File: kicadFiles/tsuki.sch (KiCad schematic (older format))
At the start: 332 parts, among them J1 TYPE-C-31-M12_13, J2 Conn_01x14, J3 Conn_ARM_JTAG_SWD_10, Q1 BSS138, Q2 AO4407A, SW1 ESC, SW10 9, SW11 0, SW12 -_, SW13 +=, SW14 2U BKSP, SW15 TAB_150, SW16 Q, SW17 W, SW18 E, SW19 R, SW2 1, SW20 T, SW21 Y, SW22 U, SW23 I, SW24 O, SW25 P, SW26 [{, SW27 ]}, SW28 \\|_150, SW29 CAPS_175, SW3 2, SW30 A, SW31 S, SW32 D, SW33 F, SW34 G, SW35 H, SW36 J, SW37 K, SW38 L, SW39 :;, SW4 3, SW40 \"', SW41 ENTER_225, SW42 LSHIFT_225, SW43 Z, SW44 X, SW45 C, SW46 V, SW47 B, SW48 N, SW49 M, SW5 4, SW50 <,, SW51 >., SW52 ?/, SW53 RSHIFT_275, SW54 LCTRL_150, SW55 LGUI_100, SW56 LALT_150, SW58 RALT_150, SW59 RGUI_150, SW6 5, SW60 RCTRL_150, SW61 FN_100, SW62 RSHIFT_175, SW63 STEPPED_CAPS_125, SW64 1U LBKSP, SW65 1U RBKSP, SW66 ISO_100, SW67 ISO_ENTER, SW68 LCTRL_125, SW69 LGUI_125, SW7 6, SW70 LGUI_100, SW71 LALT_125, SW72 LALT_150, SW75 SPACE_625, SW77 SPACE_700, SW8 7, SW80 RALT_125, SW81 RALT_150, SW83 RGUI_125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

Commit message: Finished routing
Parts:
- removed RL47: 420R, acheron_Components:R_SMD_1206, symbol Device:R_Small
- added L10: Tsuki Big Logo, tsukiGraphics:tsukiLogo_90x115mm, symbol Mechanical:MountingHole
- added LED49, LED50, LED51, LED52, LED53, LED54, LED55, LED56, LED57, LED58, LED59, LED60, LED61, LED62, LED63, LED64, LED65, LED66, LED67, LED68, LED69, LED70, LED71, LED72, LED73, LED74, LED75, LED76, LED77, LED78, LED79, LED80, LED81: LED, acheron_Components:LED_THT_2.54mm, symbol tsuki-rescue:LED-acheronSymbols
- added RL48, RL49, RL50, RL51, RL52, RL53, RL54, RL55, RL56, RL57, RL58, RL60, RL61, RL63, RL66, RL68, RL69, RL71, RL73, RL75, RL77: 420R, acheron_Components:R_SMD_1206, symbol Device:R_Small
- renumbered CRST1 to CR1, CRST2 to CR2, DRST1 to DR1, RRST1 to RR1, SWRST1 to SWR1
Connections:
- wire segments 709 -> 830
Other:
- moved on the sheet: D66, LED31, LED32, LED33, LED34, LED35, LED36, LED37, LED38, LED39, LED40, LED41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

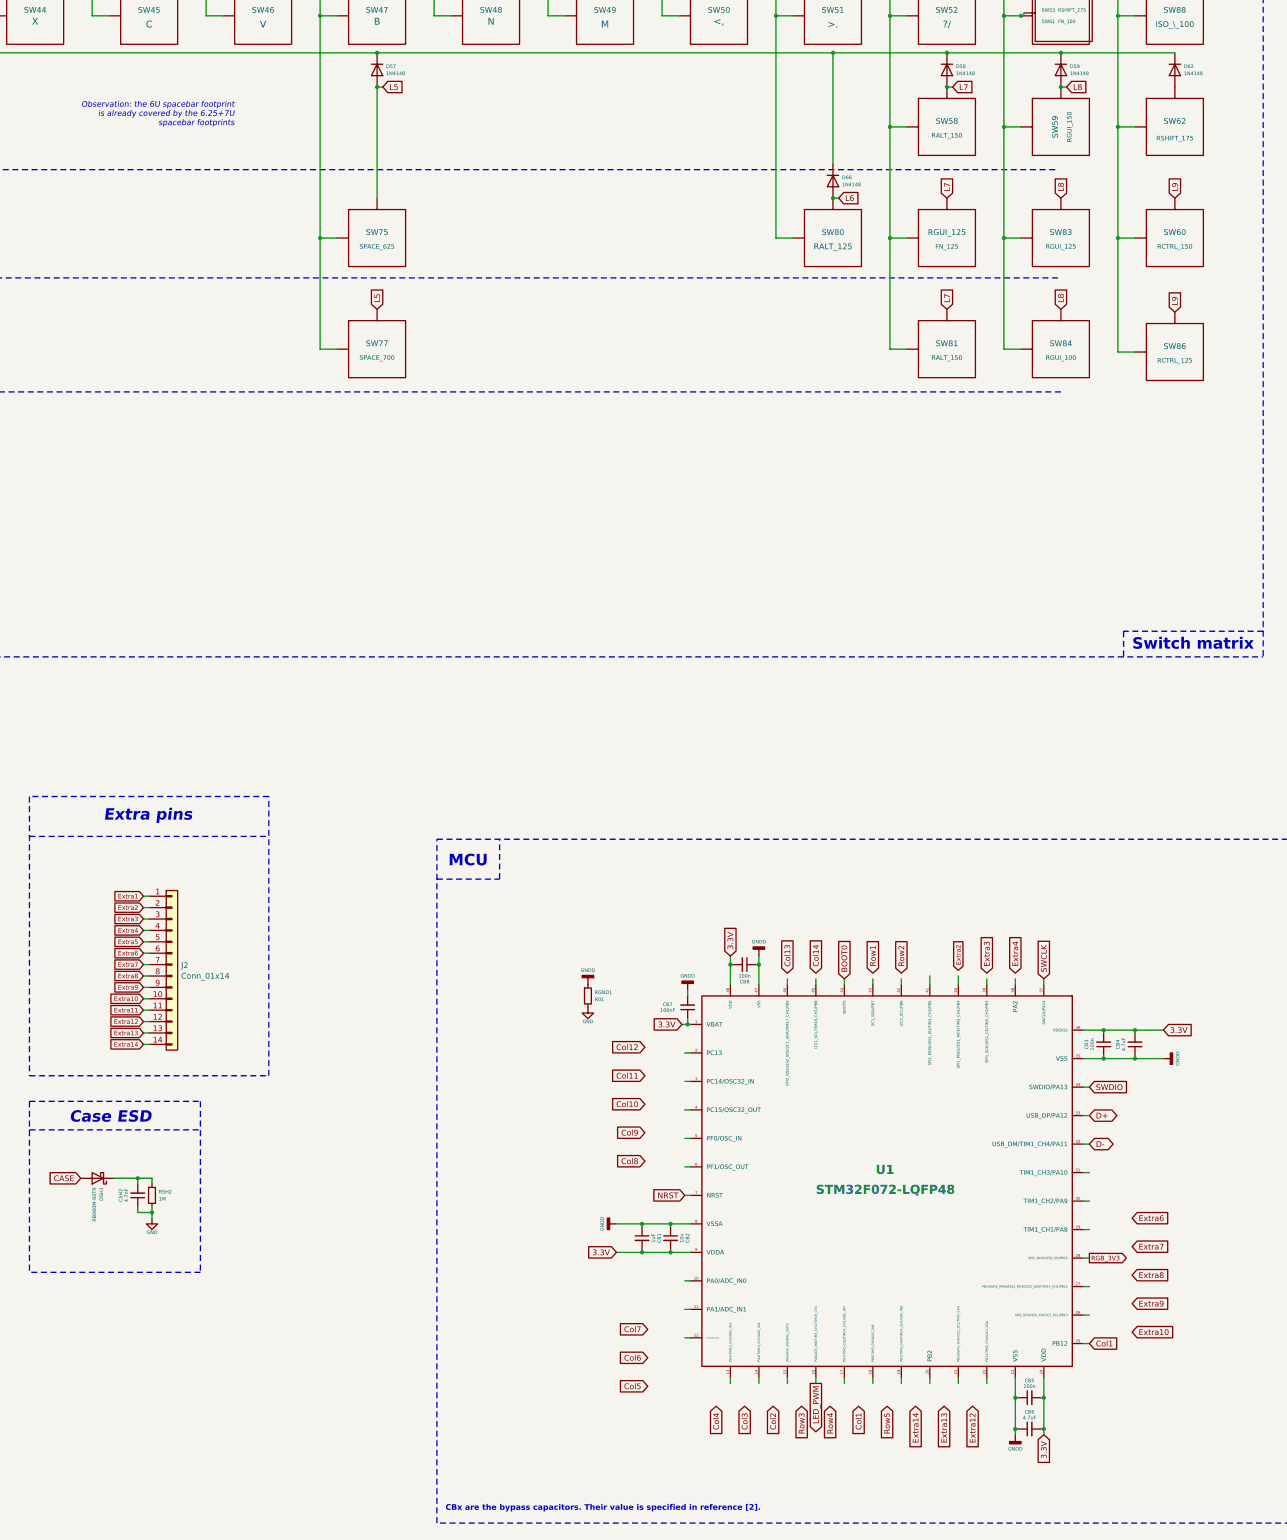
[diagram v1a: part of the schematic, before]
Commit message: Assign col and row pins
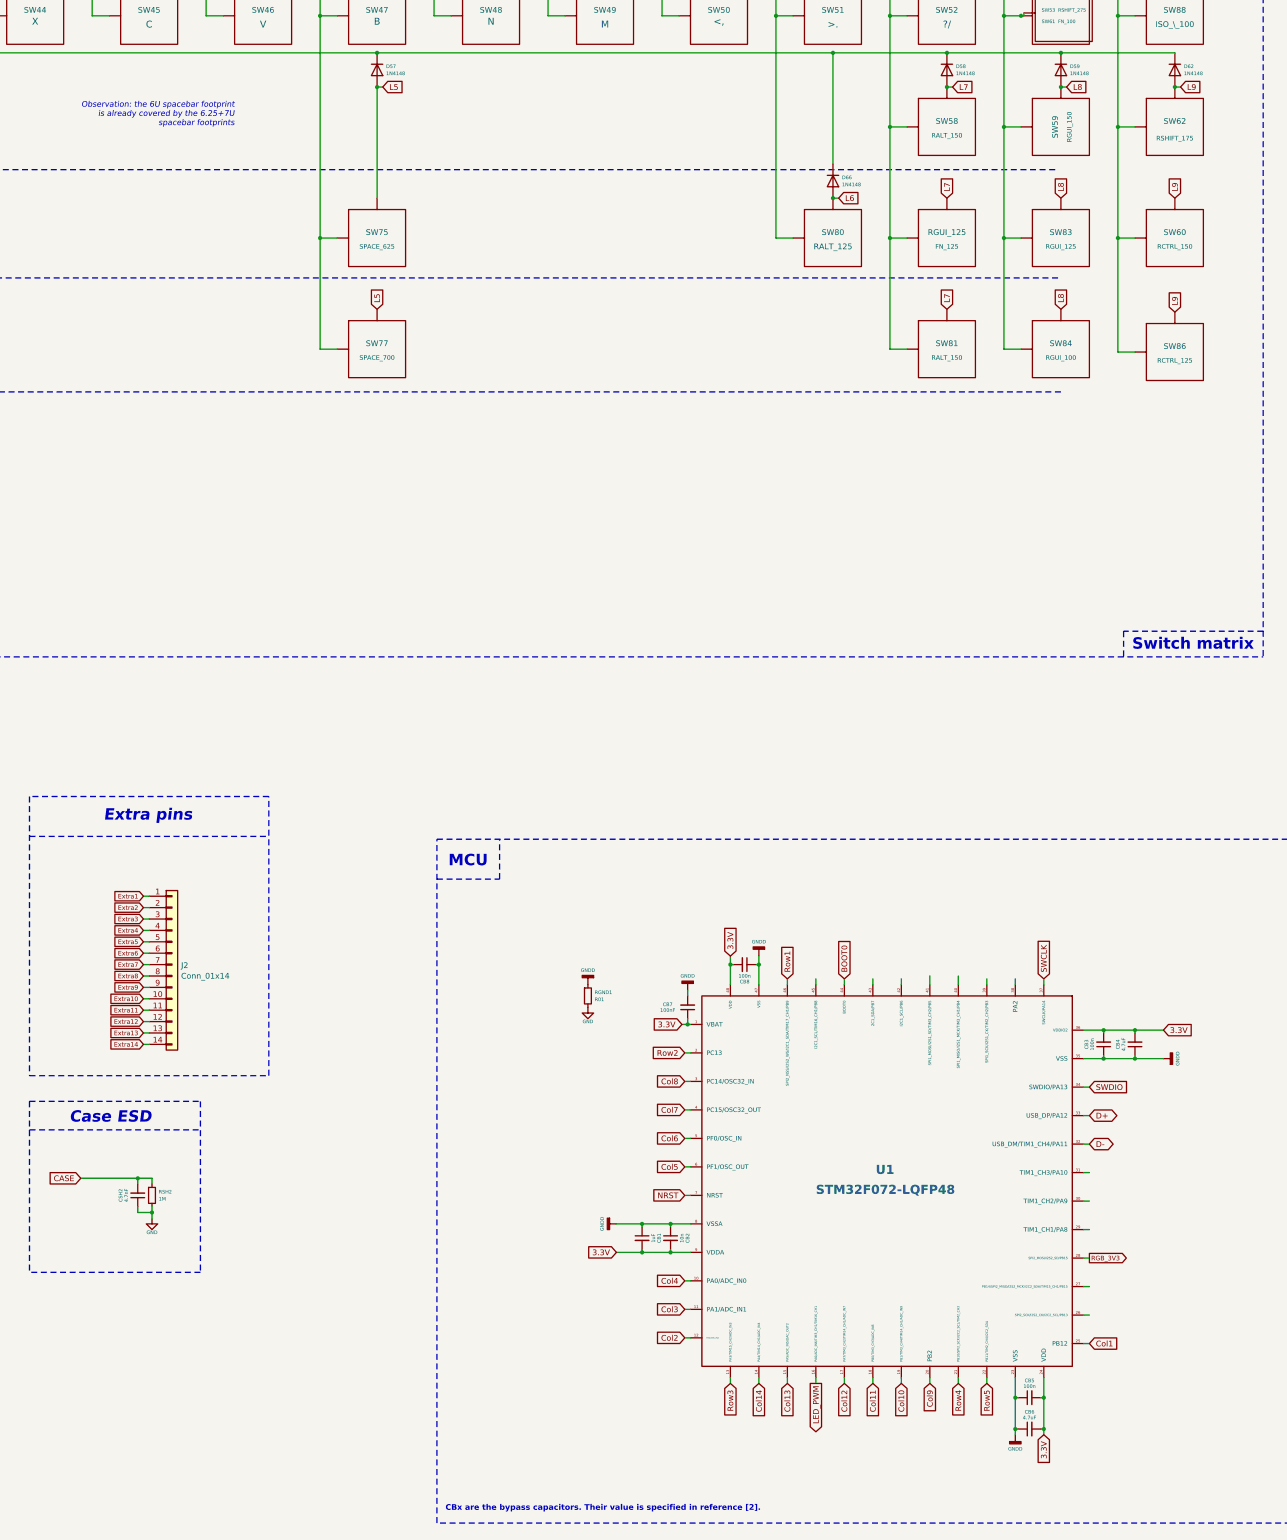
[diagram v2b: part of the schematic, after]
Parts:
- removed DSH1: RB060M-60TR, acheron_Components:D_SOD-123, symbol Device:D_Schottky
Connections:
- wire segments 830 -> 831

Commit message: Run DRC, finish pin assignment
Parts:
- removed L9: Warning, acheron_Graphics:warning_sign_3.6x3.2mm, symbol Mechanical:MountingHole
- added CR3, CR4: 100n, Capacitor_SMD:C_0805_2012Metric, symbol Device:C_Small
- added D60: 1N4148, acheron_Components:D_SOD-123, symbol Device:D
- added ROT1: Rotary_Encoder_Switch, acheron_Hardware:ALPS_EC11E, symbol Device:Rotary_Encoder_Switch
- added RR2, RR3, RR4, RR5: 10k, acheron_Components:R_SMD_1206, symbol Device:R_Small
- J2: value Conn_01x14 -> Conn_01x12; footprint acheron_Connectors:PinHeader_1x14_P2.54mm_Vertical -> acheron_Connectors:PinHeader_1x12_P2.54mm_Vertical; symbol Connector_Generic:Conn_01x14 -> Connector_Generic:Conn_01x12
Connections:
- net 3.3V: now also RR2.1, RR4.1
- net Col10: now also SW80.1 (Col)
- net Col11: now also RGUI_125.1 (Col), SW58.1 (Col), SW81.1 (Col); no longer SW80.1 (Col)
- net Col12: now also SW59.2 (Row), SW83.1 (Col), SW84.1 (Col); no longer RGUI_125.1 (Col), SW58.1 (Col), SW81.1 (Col)
- net Col13: now also SW60.1 (Col), SW62.1 (Col), SW86.1 (Col); no longer SW59.2 (Row), SW61.1 (Col), SW83.1 (Col), SW84.1 (Col)
- net Col14: now also SW61.1 (Col), ROT1.S2; no longer SW60.1 (Col), SW62.1 (Col), SW86.1 (Col)
- net Extra1: now also U1.45 (I2C1_SCL/TIM16_CH1/PB8)
- net Extra10: now also U1.29 (TIM1_CH1/PA8)
- net Extra11: now also U1.27 (PB14/SPI2_MISO/I2S2_MCK/I2C2_SDA/TIM15_CH1/PB15)
- net Extra12: now also U1.26 (SPI2_SCK/I2S2_CK/I2C2_SCL/PB13)
- net Extra2: now also U1.43 (2C1_SDA/PB7)
- net Extra3: now also U1.42 (I2C1_SCL/PB6)
- net Extra4: now also U1.41 (SPI1_MOSI/I2S1_SD/TIM3_CH2/PB5)
- net Extra5: now also U1.40 (SPI1_MISO/I2S1_MCK/TIM3_CH1/PB4)
- net Extra6: now also U1.39 (SPI1_SCK/I2S1_CK/TIM2_CH2/PB3)
- net Extra7: now also U1.38 (PA2)
- net Extra8: now also U1.31 (TIM1_CH3/PA10)
- net Extra9: now also U1.30 (TIM1_CH2/PA9)
- net GND: now also CR3.2, CR4.2, ROT1.C
- net L9: now also D60.2 (A); no longer D62.2 (A), SW62.2 (Row)
- net Row5: now also D60.1 (K)
- net at D53.2 (A), SW53.2 (Row): now also SW62.2 (Row); no longer SW61.2 (Row)
- removed net Extra13: J2.13 (Pin_13)
- removed net Extra14: J2.14 (Pin_14)
- new net ENC_A: CR3.1, RR3.2
- new net ENC_B: CR4.1, RR5.2
- new net ROT_A: ROT1.A, RR2.2, RR3.1
- new net ROT_B: ROT1.B, RR4.2, RR5.1
- new net ROT_S1: D62.2 (A), ROT1.S1, SW61.2 (Row)
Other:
- moved on the sheet: D58, D59, D66, RGUI_125, SW58, SW59, SW60, SW61, SW62, SW80, SW81, SW83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

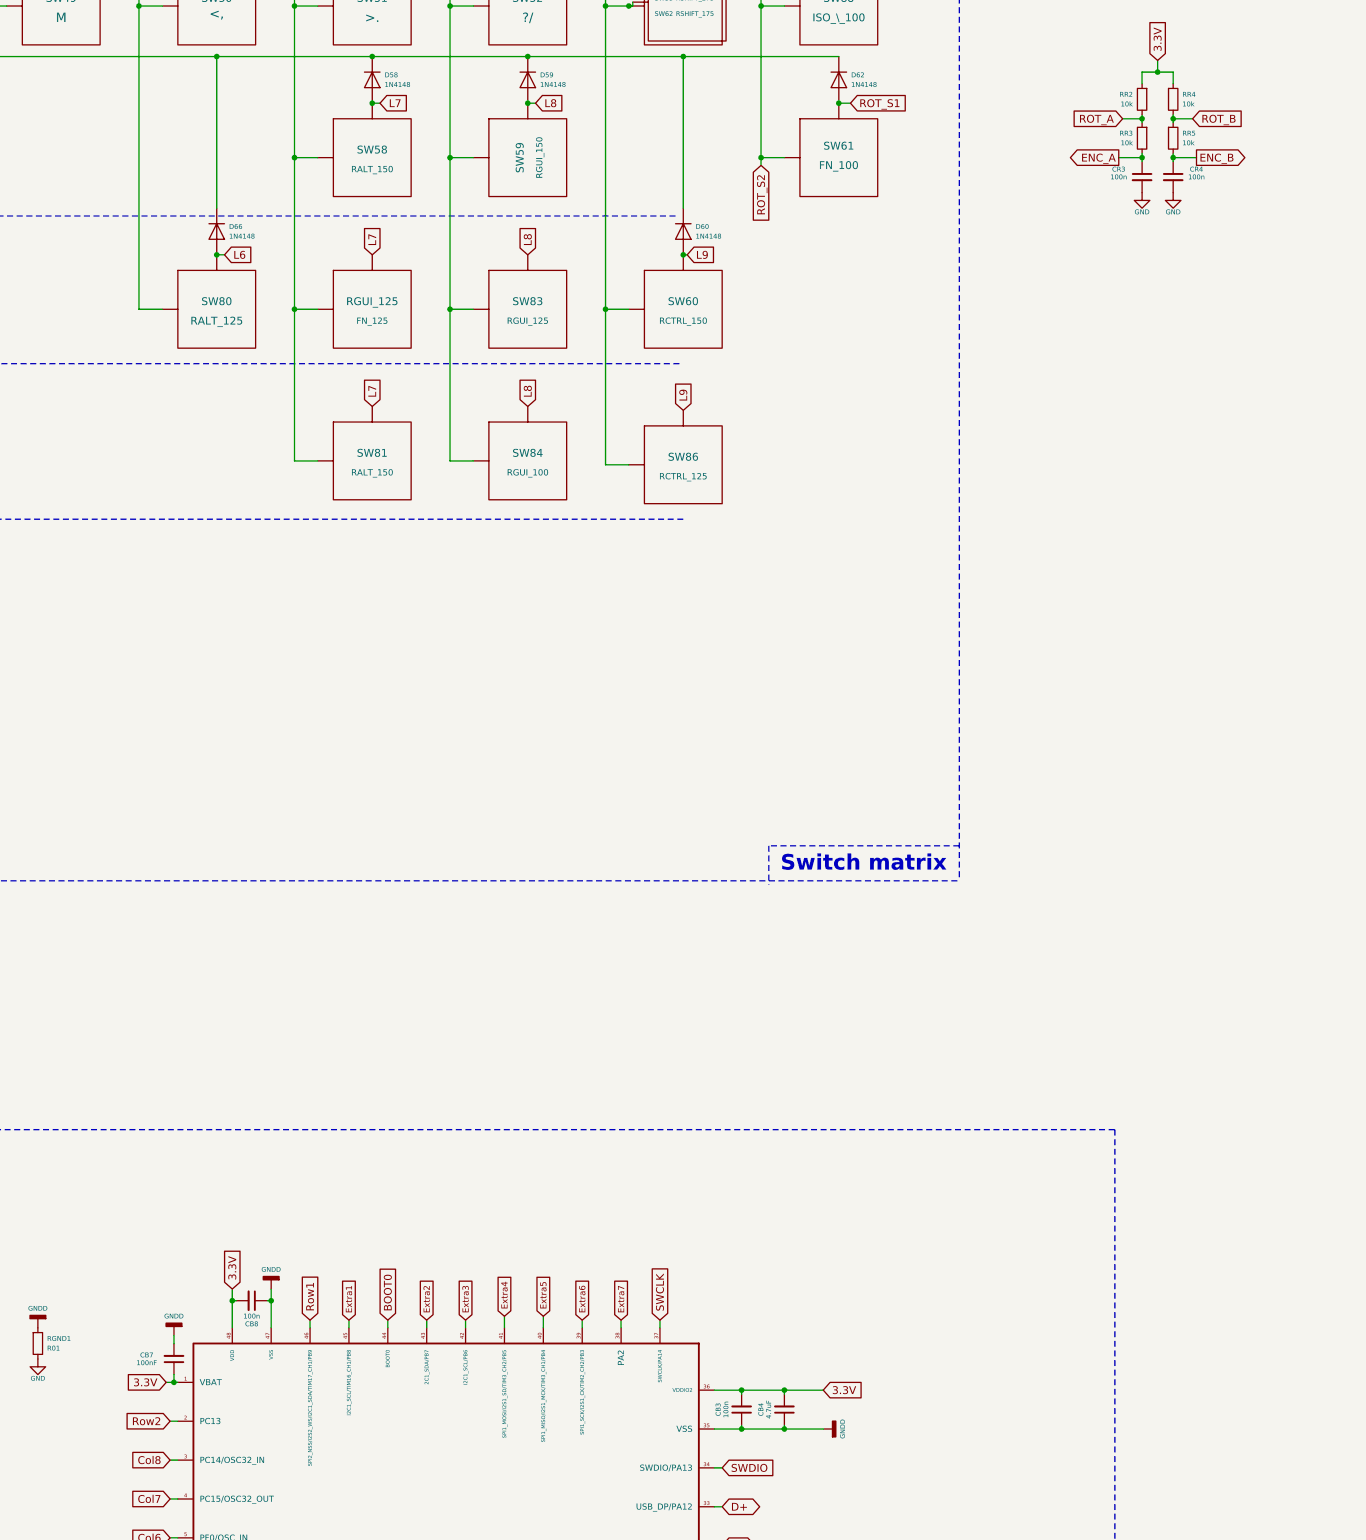
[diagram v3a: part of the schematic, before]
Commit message: Add rotary encoder support
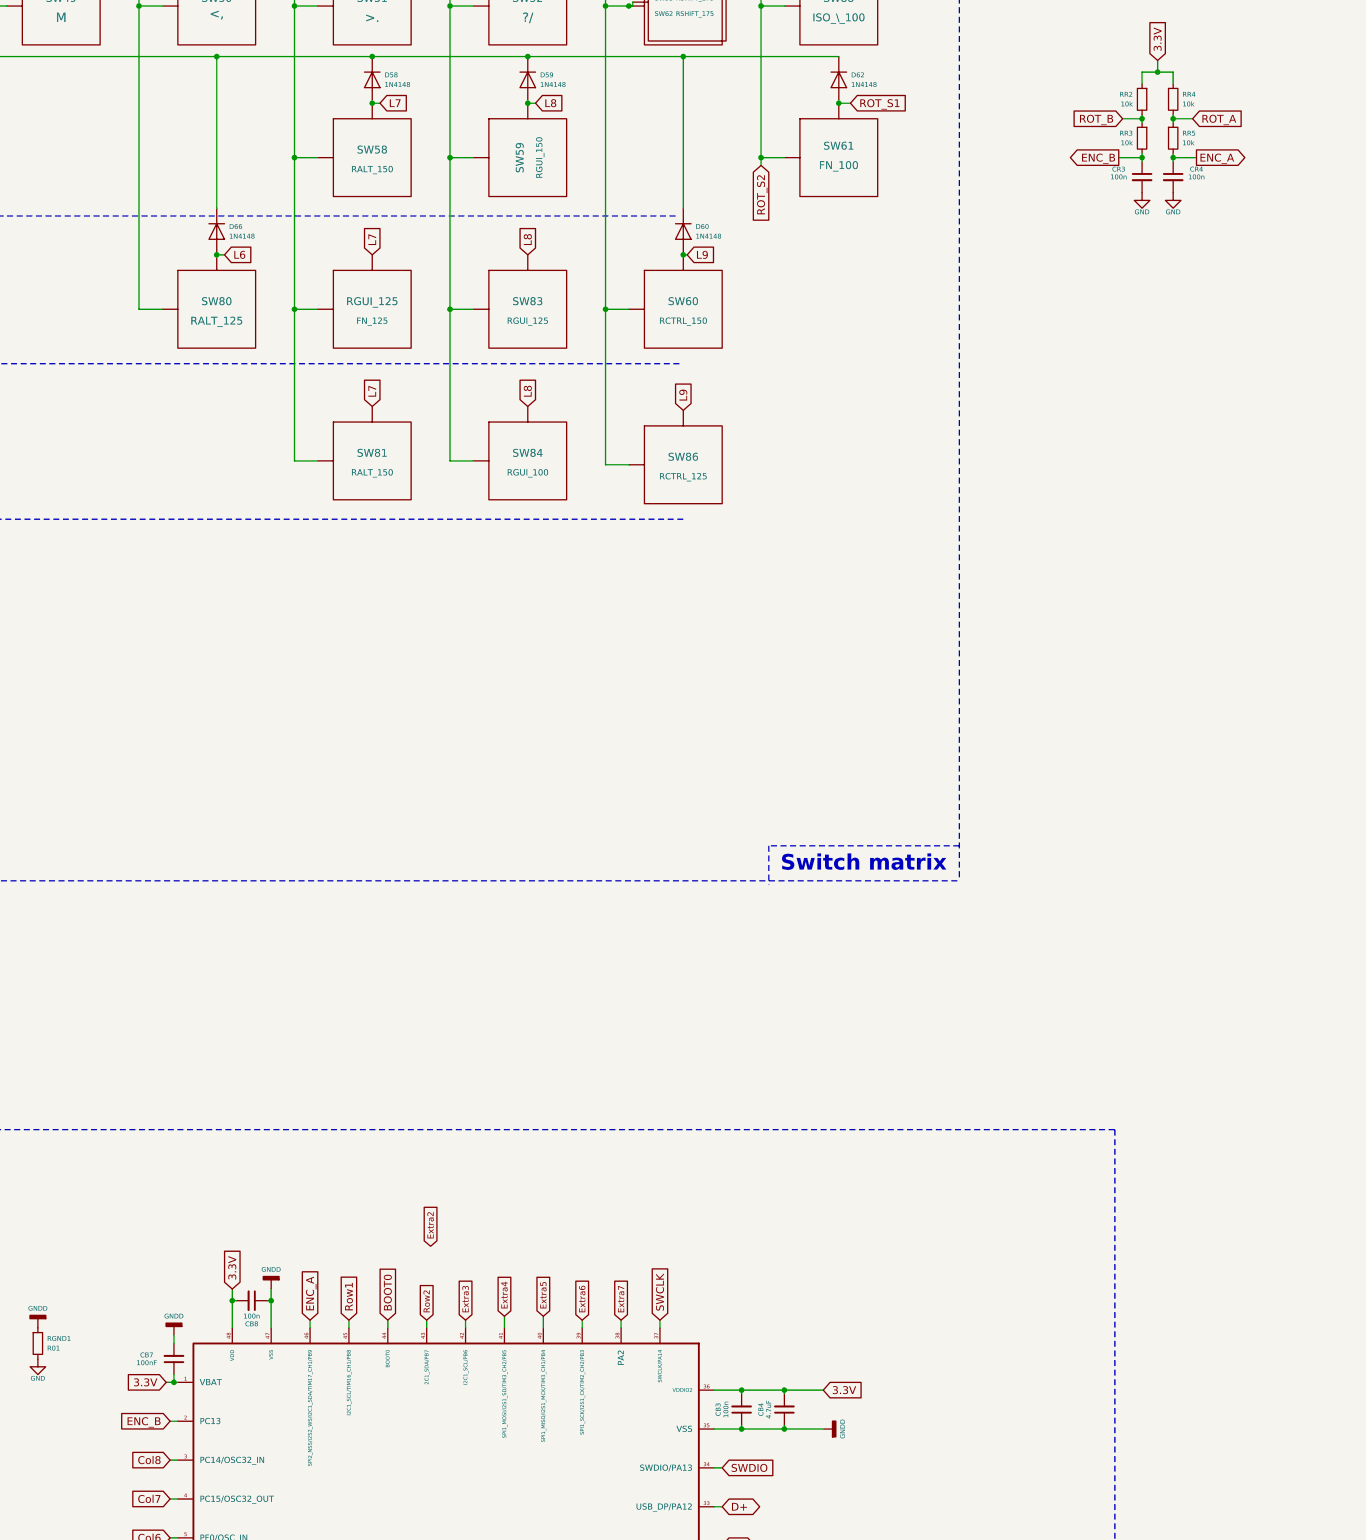
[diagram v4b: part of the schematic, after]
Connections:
- net ENC_A: now also CR4.1, RR5.2, U1.46 (SPI2_NSS/I2S2_WS/I2C1_SDA/TIM17_CH1/PB9); no longer CR3.1, RR3.2
- net ENC_B: now also CR3.1, RR3.2, U1.2 (PC13); no longer CR4.1, RR5.2
- net Extra1: no longer U1.45 (I2C1_SCL/TIM16_CH1/PB8)
- net Extra2: no longer U1.43 (2C1_SDA/PB7)
- net ROT_A: now also RR4.2, RR5.1; no longer RR2.2, RR3.1
- net ROT_B: now also RR2.2, RR3.1; no longer RR4.2, RR5.1
- net Row1: now also U1.45 (I2C1_SCL/TIM16_CH1/PB8); no longer U1.46 (SPI2_NSS/I2S2_WS/I2C1_SDA/TIM17_CH1/PB9)
- net Row2: now also U1.43 (2C1_SDA/PB7); no longer U1.2 (PC13)
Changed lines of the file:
@@
 Wire Wire Line
 	11425 17250 11925 17250
-Text GLabel 16725 16150 0    50   Input ~ 0
-Row2
+Text GLabel 17625 15500 1    50   Input ~ 0
+ENC_A
 Text GLabel 16725 18400 0    50   Input ~ 0
 Col3
@@
 Text GLabel 19375 19050 3    50   Input ~ 0
 Row5
-Text GLabel 17625 15500 1    50   Input ~ 0
+Text GLabel 17875 15500 1    50   Input ~ 0
 Row1
 Text GLabel 17375 19050 3    50   Input ~ 0
@@
 Text GLabel 20275 17450 2    40   Input ~ 0
 Extra9
-Text GLabel 17875 15500 1    40   Input ~ 0
-Extra1
 Text GLabel 18375 15500 1    40   Input ~ 0
+Row2
+Text GLabel 18400 15025 1    40   Input ~ 0
 Extra2
 Connection ~ 16525 7050
@@
 	23075 7475 23175 7475
 Text GLabel 22850 7775 0    50   Input ~ 0
-ROT_A
+ROT_B
 Wire Wire Line
 	22975 8050 22975 8025
@@
 	22975 7775 22975 7750
 Text GLabel 23300 7775 2    50   Input ~ 0
-ROT_B
+ROT_A
 Wire Wire Line
 	23300 7775 23175 7775
@@
 	23075 6675 23250 6675
 Text GLabel 22825 8025 0    50   Output ~ 0
-ENC_A
+ENC_B
 Wire Wire Line
 	22825 8025 22975 8025
@@
 	22975 8025 22975 8000
 Text GLabel 23325 8025 2    50   Output ~ 0
-ENC_B
+ENC_A
 Wire Wire Line
 	23325 8025 23175 8025
@@
 Wire Wire Line
 	23175 8025 23175 8000
+Text GLabel 16725 16150 0    50   Input ~ 0
+ENC_B
 $EndSCHEMATC

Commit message: Refreshed renders and KLE
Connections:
- net 5V: now also Q2.1 (S), Q2.2 (S), Q2.3 (S); no longer Q2.5 (D), Q2.6 (D), Q2.7 (D), Q2.8 (D)
- net at RL1.2, RL10.2, RL11.2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: now also Q2.5 (D), Q2.6 (D), Q2.7 (D), Q2.8 (D); no longer Q2.1 (S), Q2.2 (S), Q2.3 (S)
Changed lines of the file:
@@
 F 3 "" H -6525 11000 50  0001 C CNN
 	1    -6425 11000
-	1    0    0    -1
+	1    0    0    1
 $EndComp
 $Comp
